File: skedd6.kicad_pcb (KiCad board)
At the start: 2 copper layers, 25.4 x 27.9 mm, 12 parts, among them J1 Conn_02x10_Odd_Even, J2 Conn_02x03_Odd_Even, J3 Conn_01x03_Pin, J4 Conn_01x03_Pin, J5 Conn_01x02_Pin, J6 Conn_01x02_Pin, U1 AMS1117-3.3

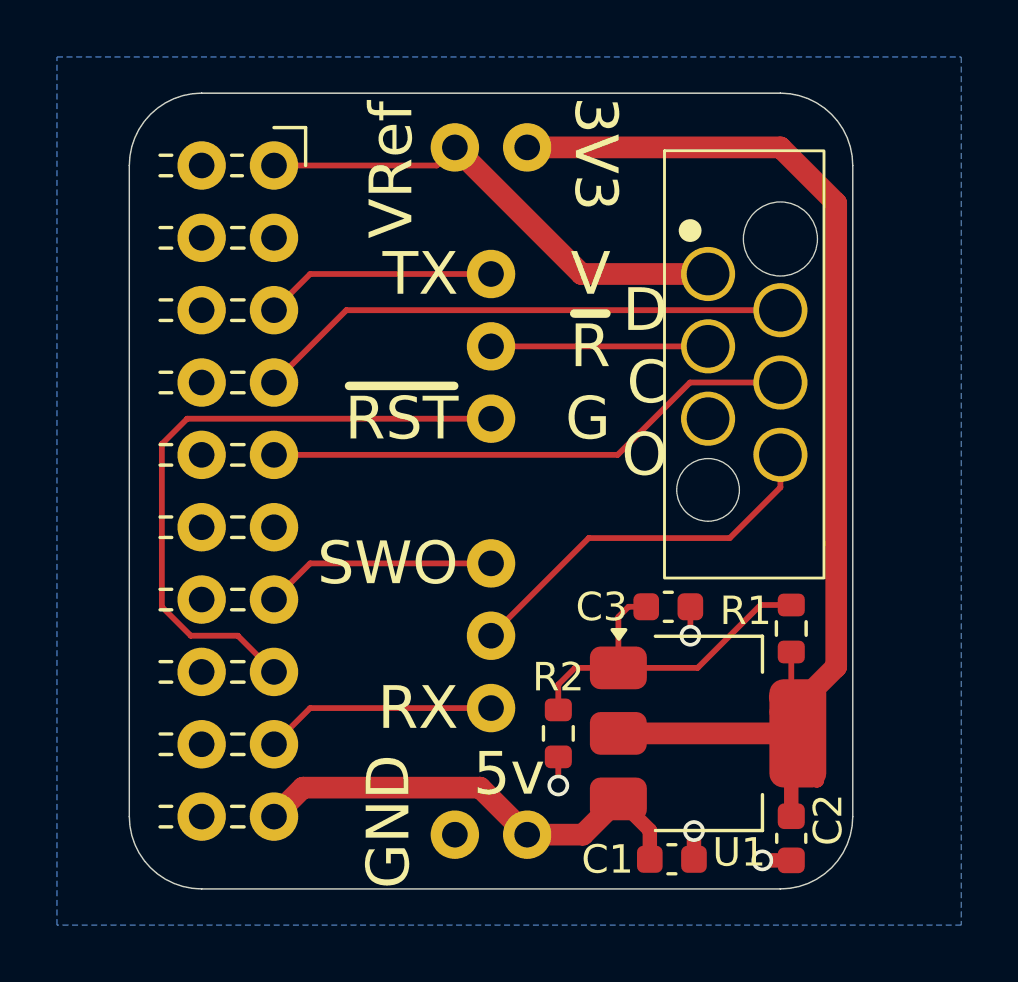
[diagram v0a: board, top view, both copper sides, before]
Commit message: Version with AP7362 LDO
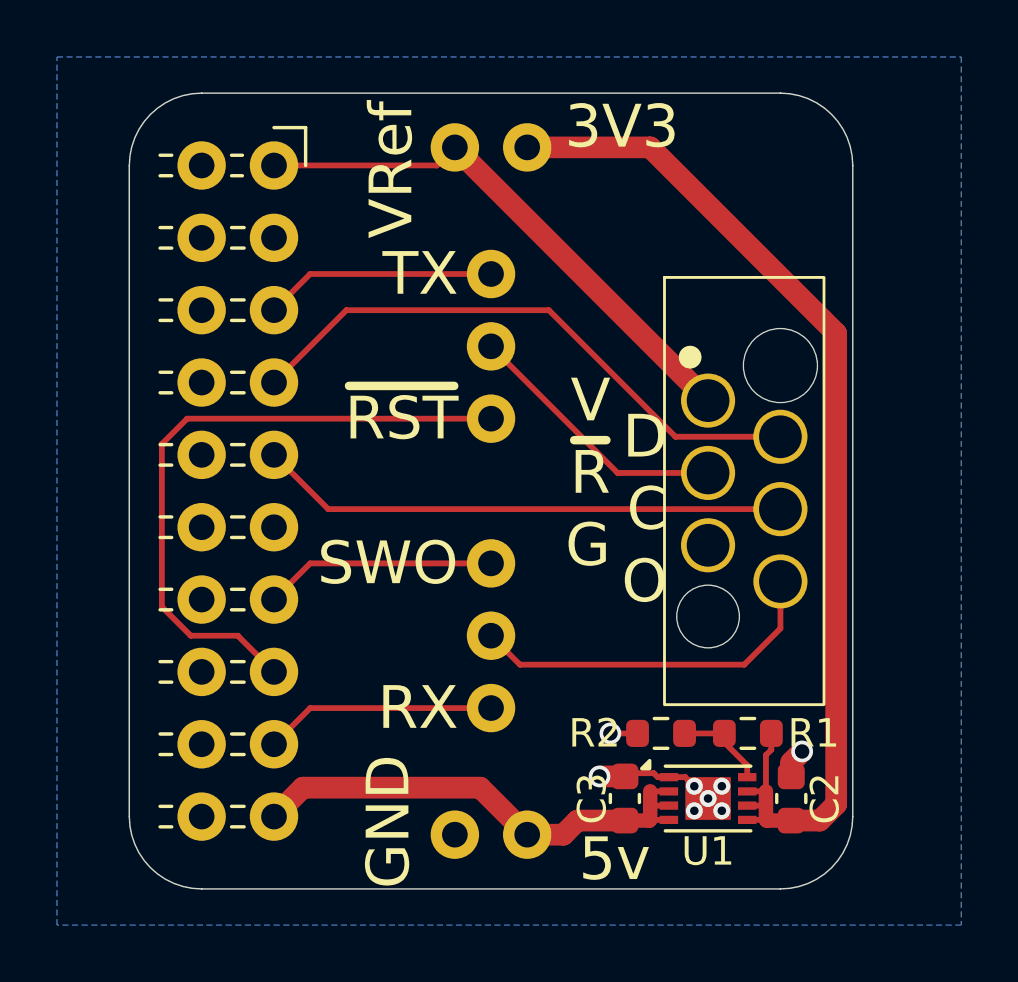
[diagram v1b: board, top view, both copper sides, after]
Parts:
- removed C1: 10u, Capacitor_SMD:C_0603_1608Metric
- R1: value R -> 45k
- R2: value 0 -> 10k
- U1: value AMS1117-3.3 -> AP7363-HA; footprint Parts:SOT-223-3_TabPin2 -> Parts:DFN-8-1EP_3x2mm_P0.5mm_EP1.6x1.5mm
- moved C3 6.90 mm to (63.1, 73.0), turned to -90 degrees
- moved J2 4.45 mm to (67.3, 62.2)
- moved R1 3.99 mm to (67.4, 70.7), turned to 180 degrees
- moved R2 3.61 mm to (64.4, 70.7), turned to 0 degrees
- moved U1 2.29 mm to (66.0, 73.0)
- moved C2 1.40 mm to (69.0, 73.0)
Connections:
- C2 pad 1: +3.3V -> GND
- C2 pad 2: GND -> +3.3V
- C3 pad 2: Net-(U1-GND) -> +5V
- R1 pad 2: Net-(U1-GND) -> Net-(U1-ADJ)
- R2 pad 2: Net-(U1-GND) -> Net-(U1-ADJ)
- U1 pad 1: Net-(U1-GND) -> GND
- U1 pad 2: +3.3V -> +5V
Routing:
- net Net-(U1-GND): track 13.2 -> 0.00 mm
- net +3.3V: track 46.3 -> 37.9 mm
- net Net-(U1-ADJ): track 0.00 -> 3.27 mm
- net /SkeddRST: track 7.62 -> 9.46 mm
- net /VTRef: track 17.3 -> 19.2 mm
- net /SWDIO: track 18.8 -> 20.7 mm
- net GND: track 4.14 -> 5.55 mm, vias 4 -> 8
- net +5V: track 16.3 -> 17.5 mm
- net /SkeddTX: track 13.5 -> 12.8 mm
